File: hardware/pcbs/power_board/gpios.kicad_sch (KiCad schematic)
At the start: 9 parts, among them J11 Header_02x06, U12 TCA9534

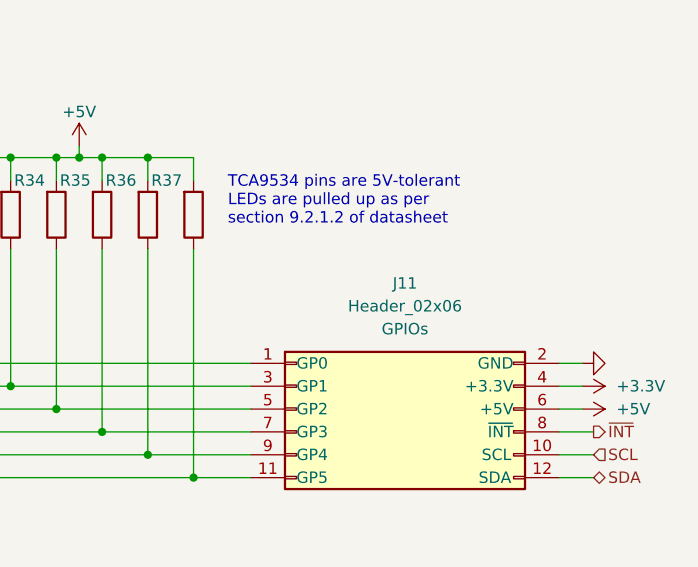
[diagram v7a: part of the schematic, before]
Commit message: power_board: THERE ARE FOUR FANS
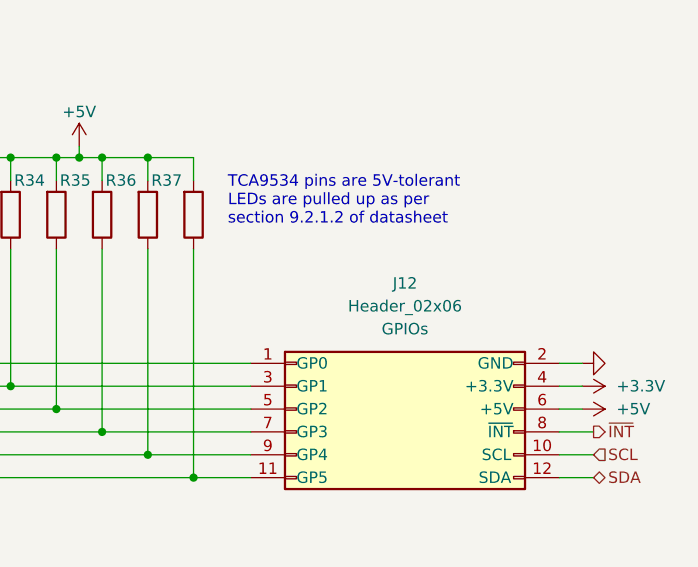
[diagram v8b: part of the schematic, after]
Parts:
- renumbered J11 to J12
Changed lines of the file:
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@@
 		(dnp no)
 		(fields_autoplaced yes)
-		(property "Reference" "#PWR043"
+		(property "Reference" "#PWR044"
 			(at 93.98 110.49 0)
 			(effects
@@
 			(project "power_board"
 				(path "/4b166175-80a4-48c6-994d-6e62a6160b87/3edd2854-0228-4fdc-a8ff-c4090a82b3f5"
-					(reference "#PWR043")
+					(reference "#PWR044")
 					(unit 1)
 				)
@@
 		(on_board yes)
 		(dnp no)
-		(property "Reference" "#PWR045"
+		(property "Reference" "#PWR046"
 			(at 104.14 88.9 0)
 			(effects
@@
 			(project "power_board"
 				(path "/4b166175-80a4-48c6-994d-6e62a6160b87/3edd2854-0228-4fdc-a8ff-c4090a82b3f5"
-					(reference "#PWR045")
+					(reference "#PWR046")
 					(unit 1)
 				)
@@
 		(on_board yes)
 		(dnp no)
-		(property "Reference" "#PWR040"
+		(property "Reference" "#PWR041"
 			(at 81.28 57.15 0)
 			(effects
@@
 			(project "power_board"
 				(path "/4b166175-80a4-48c6-994d-6e62a6160b87/3edd2854-0228-4fdc-a8ff-c4090a82b3f5"
-					(reference "#PWR040")
+					(reference "#PWR041")
 					(unit 1)
 				)
@@
 		(dnp no)
 		(fields_autoplaced yes)
-		(property "Reference" "#PWR046"
+		(property "Reference" "#PWR047"
 			(at 104.14 129.54 0)
 			(effects
@@
 			(project "power_board"
 				(path "/4b166175-80a4-48c6-994d-6e62a6160b87/3edd2854-0228-4fdc-a8ff-c4090a82b3f5"
-					(reference "#PWR046")
+					(reference "#PWR047")
 					(unit 1)
 				)
@@
 		(dnp no)
 		(fields_autoplaced yes)
-		(property "Reference" "#PWR049"
+		(property "Reference" "#PWR050"
 			(at 217.17 97.79 0)
 			(effects
@@
 			(project "power_board"
 				(path "/4b166175-80a4-48c6-994d-6e62a6160b87/3edd2854-0228-4fdc-a8ff-c4090a82b3f5"
-					(reference "#PWR049")
+					(reference "#PWR050")
 					(unit 1)
 				)
@@
 		(on_board yes)
 		(dnp no)
-		(property "Reference" "#PWR047"
+		(property "Reference" "#PWR048"
 			(at 165.1 74.93 0)
 			(effects
@@
 			(project "power_board"
 				(path "/4b166175-80a4-48c6-994d-6e62a6160b87/3edd2854-0228-4fdc-a8ff-c4090a82b3f5"
-					(reference "#PWR047")
+					(reference "#PWR048")
 					(unit 1)
 				)
@@
 		(dnp no)
 		(fields_autoplaced yes)
-		(property "Reference" "#PWR042"
+		(property "Reference" "#PWR043"
 			(at 83.82 107.95 0)
 			(effects
@@
 			(project "power_board"
 				(path "/4b166175-80a4-48c6-994d-6e62a6160b87/3edd2854-0228-4fdc-a8ff-c4090a82b3f5"
-					(reference "#PWR042")
+					(reference "#PWR043")
 					(unit 1)
 				)
@@
 		(dnp no)
 		(fields_autoplaced yes)
-		(property "Reference" "J11"
+		(property "Reference" "J12"
 			(at 201.295 86.36 0)
 			(effects
@@
 			(project "power_board"
 				(path "/4b166175-80a4-48c6-994d-6e62a6160b87/3edd2854-0228-4fdc-a8ff-c4090a82b3f5"
-					(reference "J11")
+					(reference "J12")
 					(unit 1)
 				)
@@
 		(dnp no)
 		(fields_autoplaced yes)
-		(property "Reference" "#PWR041"
+		(property "Reference" "#PWR042"
 			(at 81.28 81.28 0)
 			(effects
@@
 			(project "power_board"
 				(path "/4b166175-80a4-48c6-994d-6e62a6160b87/3edd2854-0228-4fdc-a8ff-c4090a82b3f5"
-					(reference "#PWR041")
+					(reference "#PWR042")
 					(unit 1)
 				)
@@
 		(dnp no)
 		(fields_autoplaced yes)
-		(property "Reference" "#PWR050"
+		(property "Reference" "#PWR051"
 			(at 217.17 100.33 0)
 			(effects
@@
 			(project "power_board"
 				(path "/4b166175-80a4-48c6-994d-6e62a6160b87/3edd2854-0228-4fdc-a8ff-c4090a82b3f5"
-					(reference "#PWR050")
+					(reference "#PWR051")
 					(unit 1)
 				)
@@
 		(dnp no)
 		(fields_autoplaced yes)
-		(property "Reference" "#PWR048"
+		(property "Reference" "#PWR049"
 			(at 227.33 95.25 0)
 			(effects
@@
 			(project "power_board"
 				(path "/4b166175-80a4-48c6-994d-6e62a6160b87/3edd2854-0228-4fdc-a8ff-c4090a82b3f5"
-					(reference "#PWR048")
+					(reference "#PWR049")
 					(unit 1)
 				)
@@
 		(dnp no)
 		(fields_autoplaced yes)
-		(property "Reference" "#PWR044"
+		(property "Reference" "#PWR045"
 			(at 83.82 113.03 0)
 			(effects
@@
 			(project "power_board"
 				(path "/4b166175-80a4-48c6-994d-6e62a6160b87/3edd2854-0228-4fdc-a8ff-c4090a82b3f5"
-					(reference "#PWR044")
-					(unit 1)
-				)
+					(reference "#PWR045")
+					(unit 1)
+				)
